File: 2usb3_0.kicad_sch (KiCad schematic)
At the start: 11 parts, among them J7 USB-A_USB-303WSD-BRY, U1 AP22615AWU-7

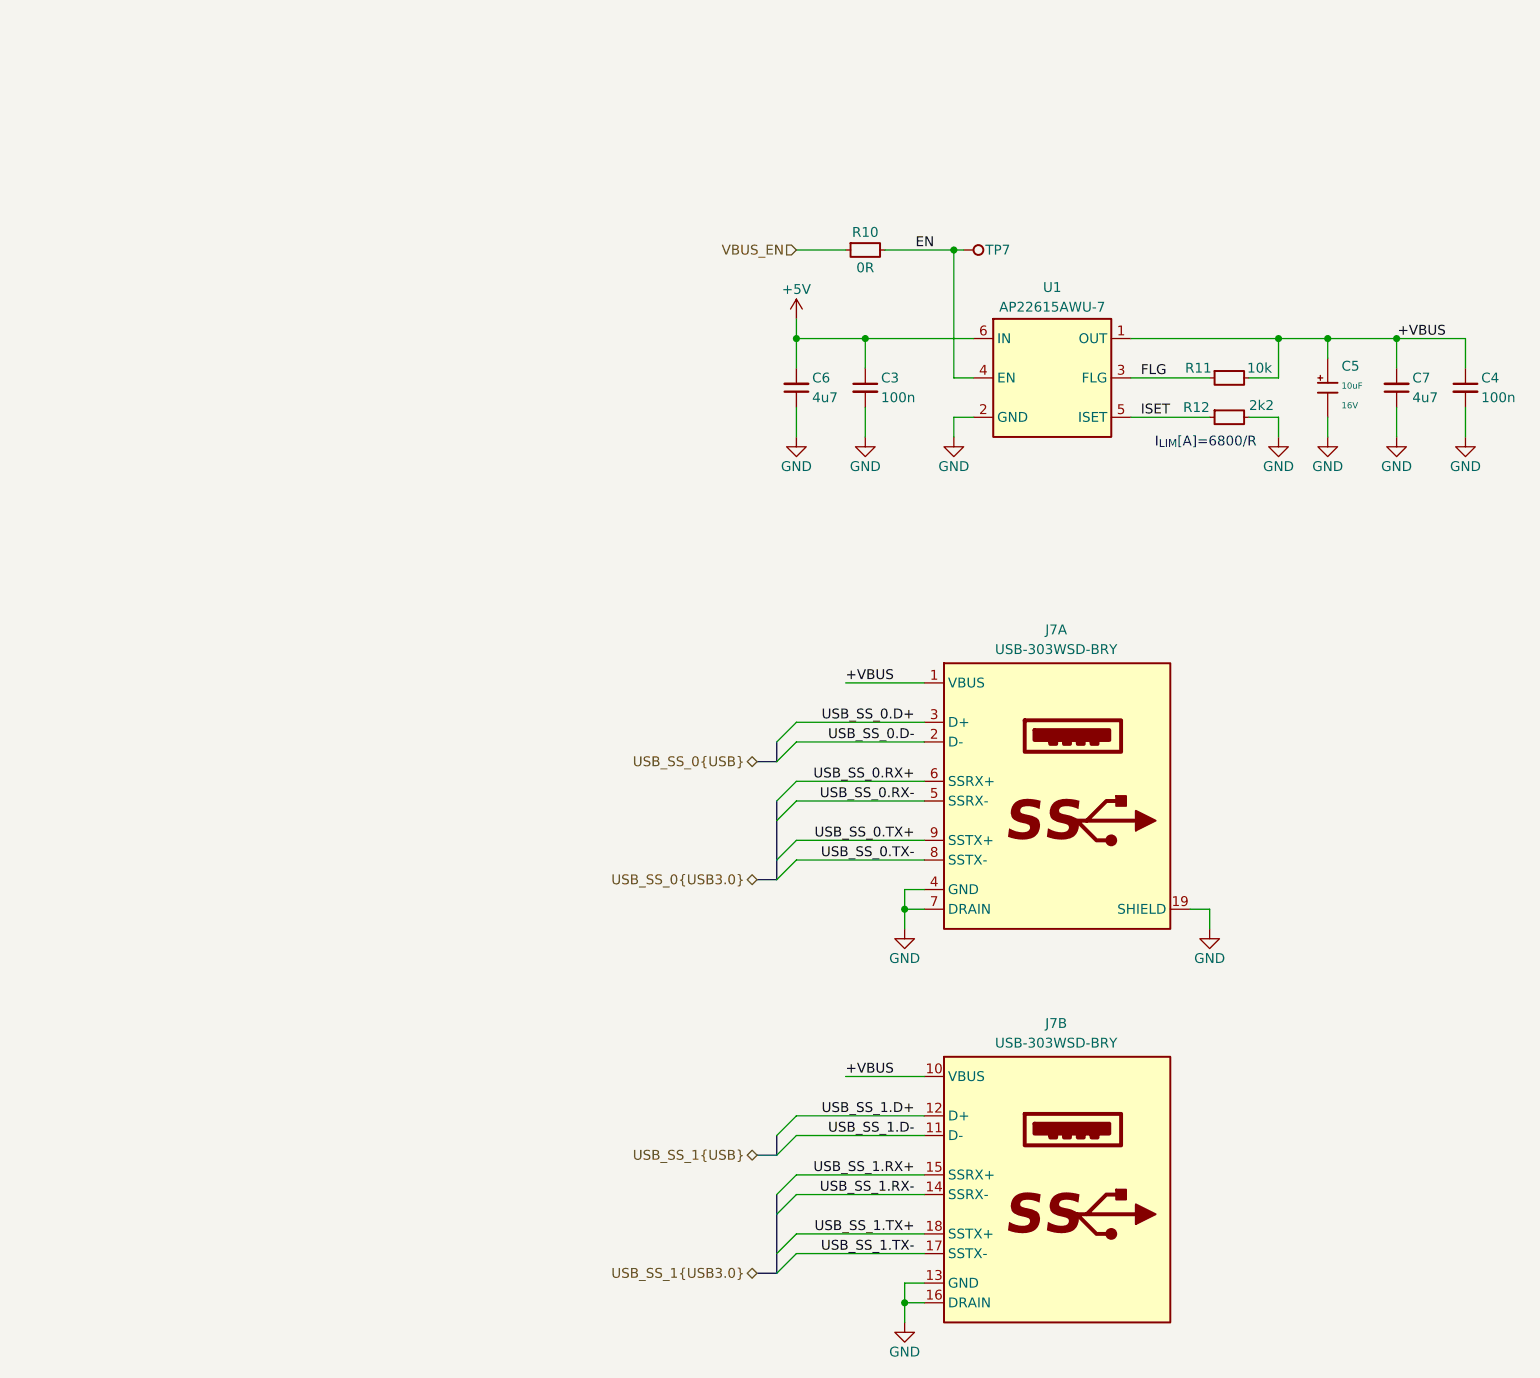
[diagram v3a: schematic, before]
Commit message: [#1] WIP: Refactor schematic
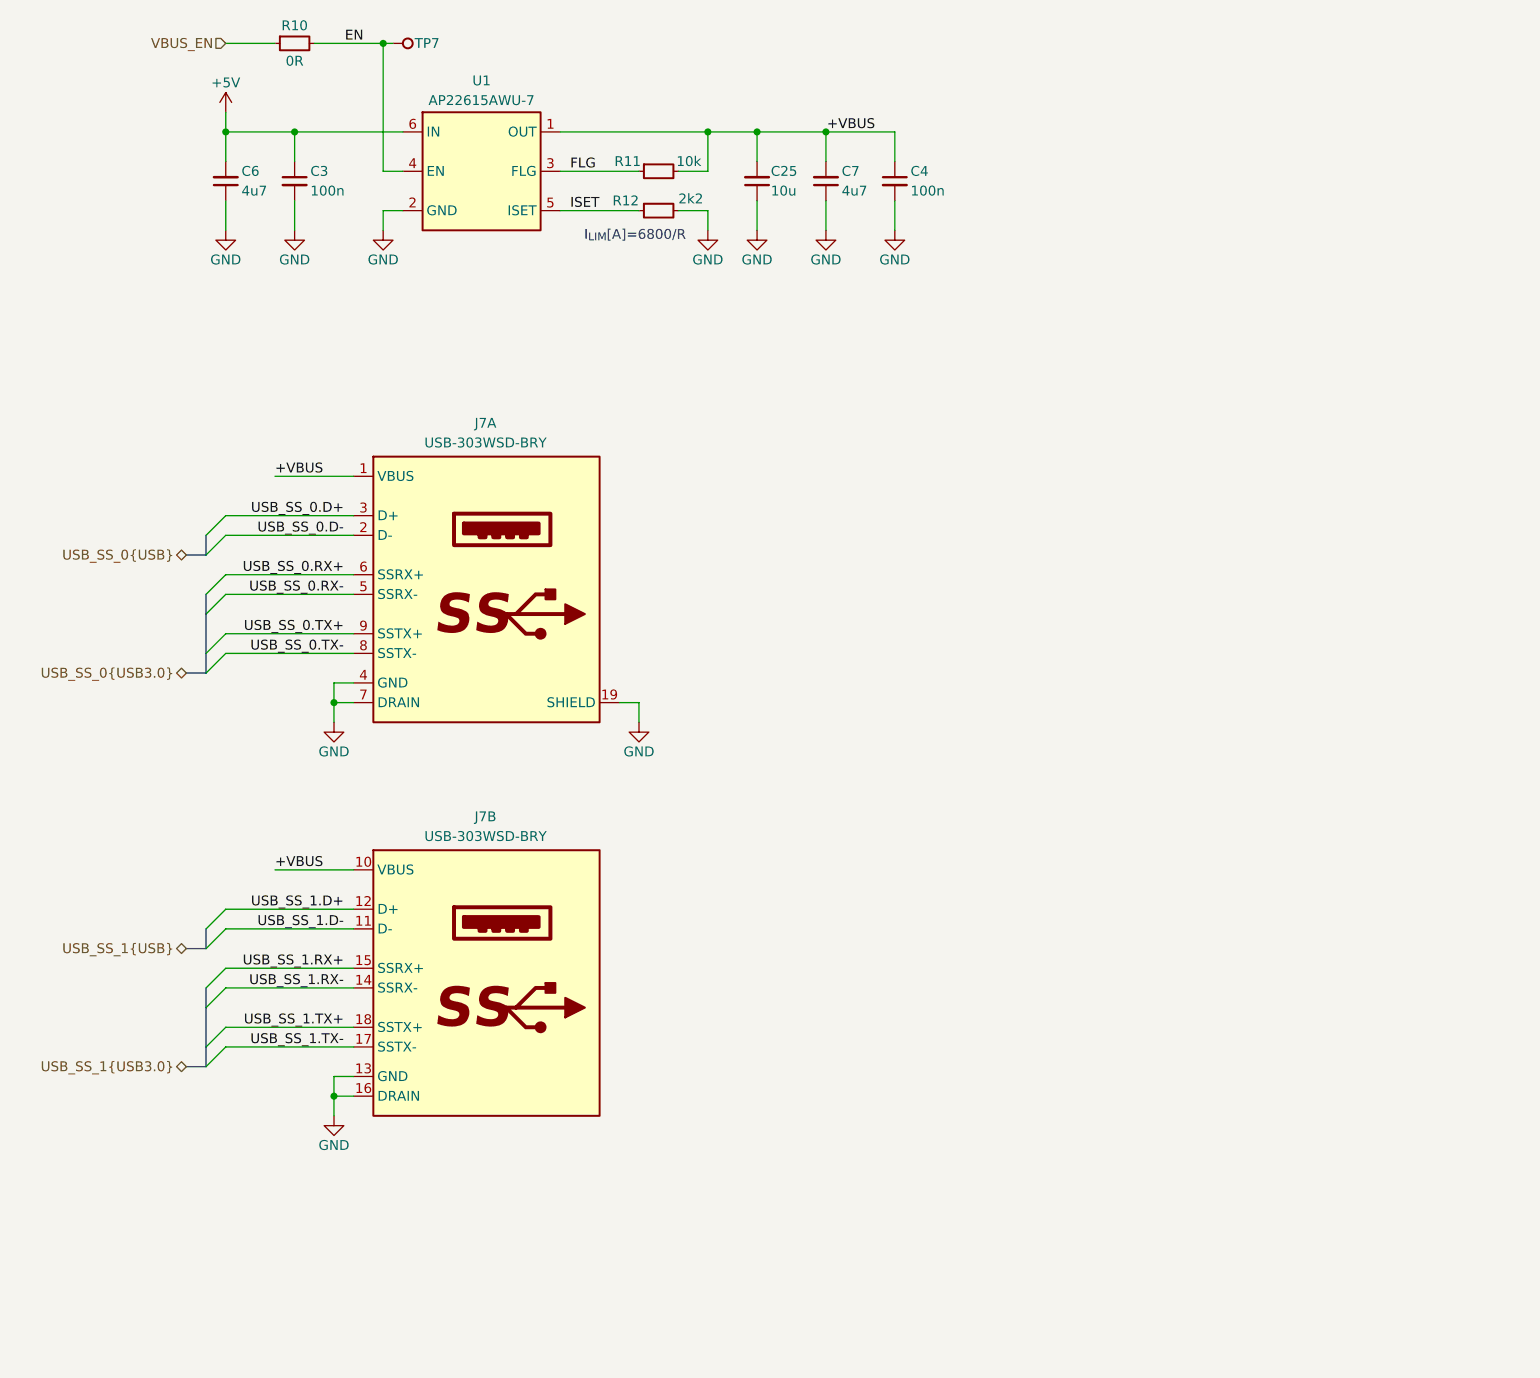
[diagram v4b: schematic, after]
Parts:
- removed C5: 10uF, PCM_JLCPCB:C_CASE-A-3216-18(mm), symbol PCM_JLCPCB-Capacitors:CASE-A-3216-18(mm),10uF
- added C25: C-10u-0603, DW-footprints:C_0603_1608Metric, symbol DW-capacitors:C-10u-0603
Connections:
- net +VBUS: now also C25.2
- net GND: now also C25.1
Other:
- moved on the sheet: C3, C4, C6, C7, J7A, J7B, R10, R11, R12, TP7, U1
